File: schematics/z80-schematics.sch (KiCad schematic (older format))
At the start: 46 parts, among them P1 FTDI SERIAL, SW1 SW_PUSH, SW2 SW_PUSH, U1 Z80-CPU, U10 Z80-CTC, U11 Z80-SIO/0, U12 74HC574, U13 74HC541, U2 AS6C1008, U3 CAT28C256BL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

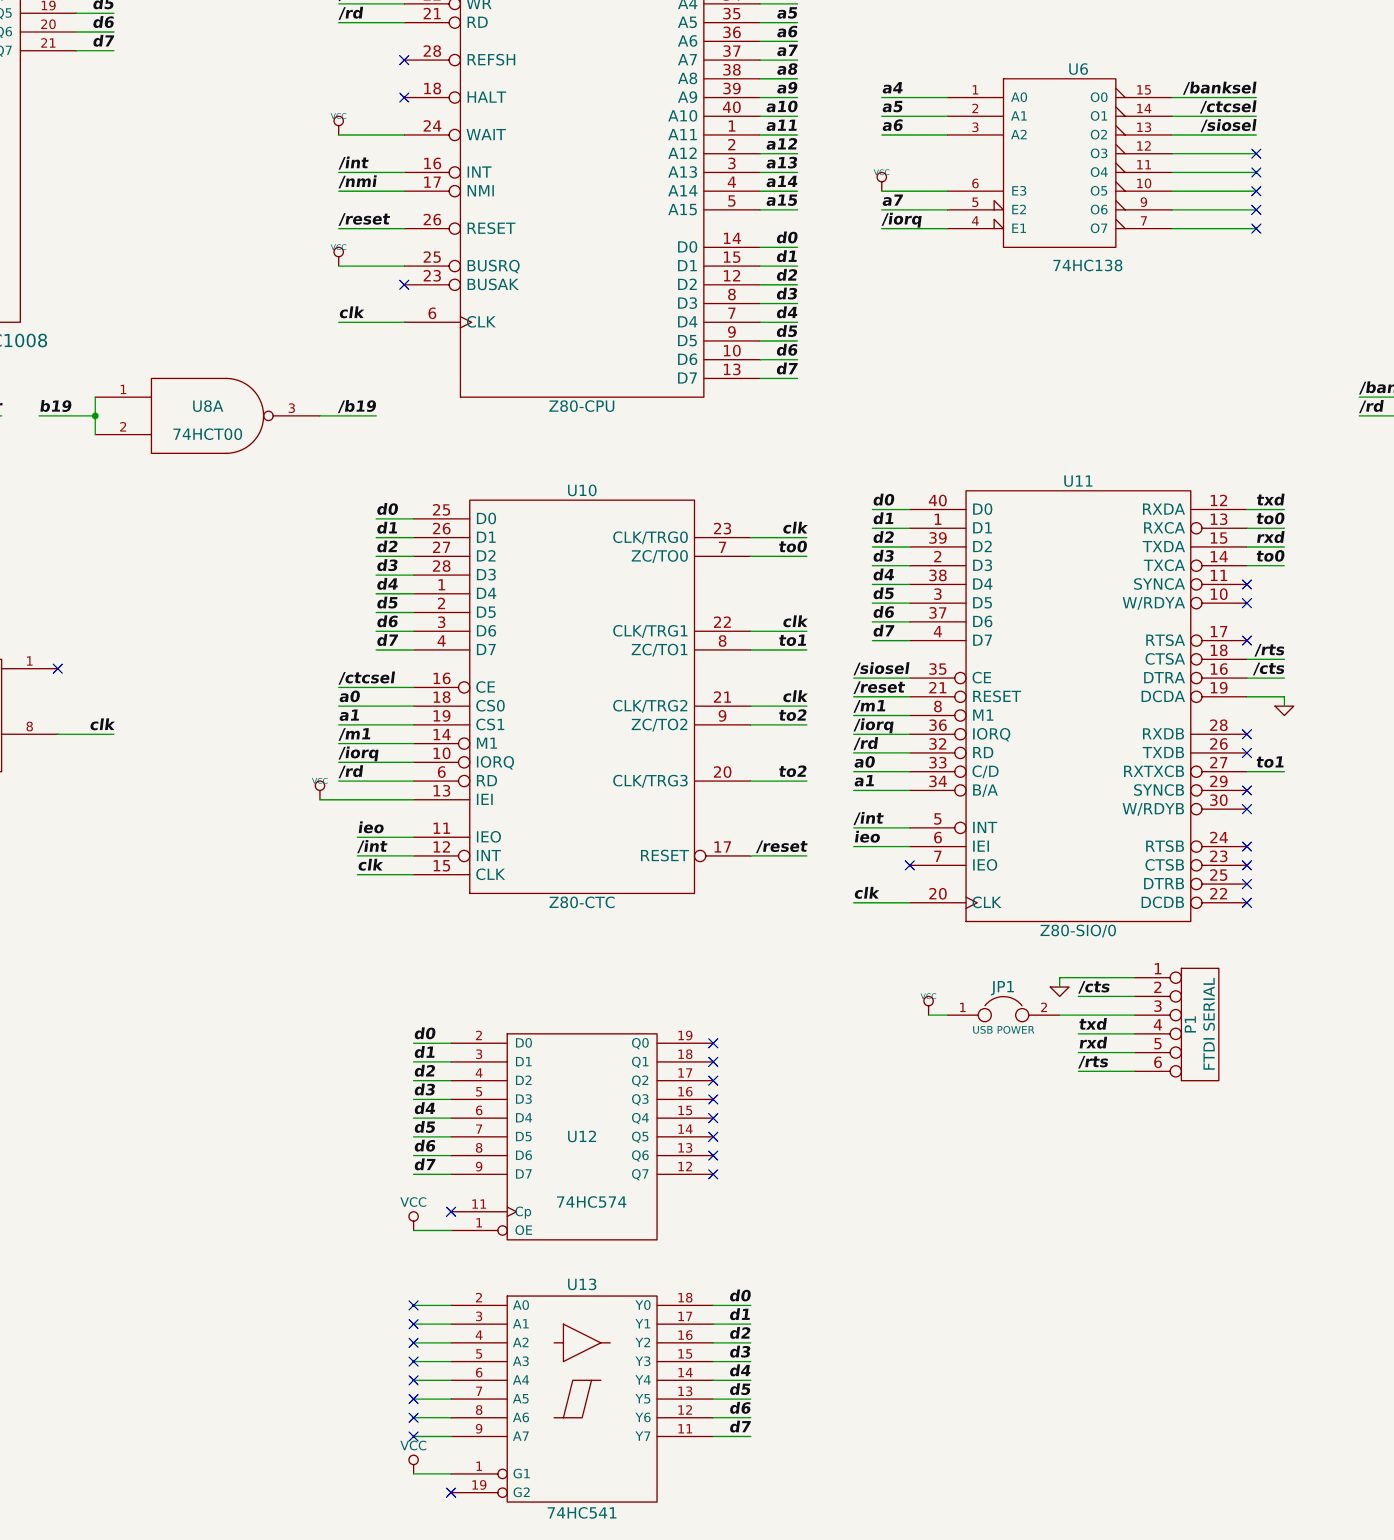
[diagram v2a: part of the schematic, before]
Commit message: Enabled parallel I/O ports
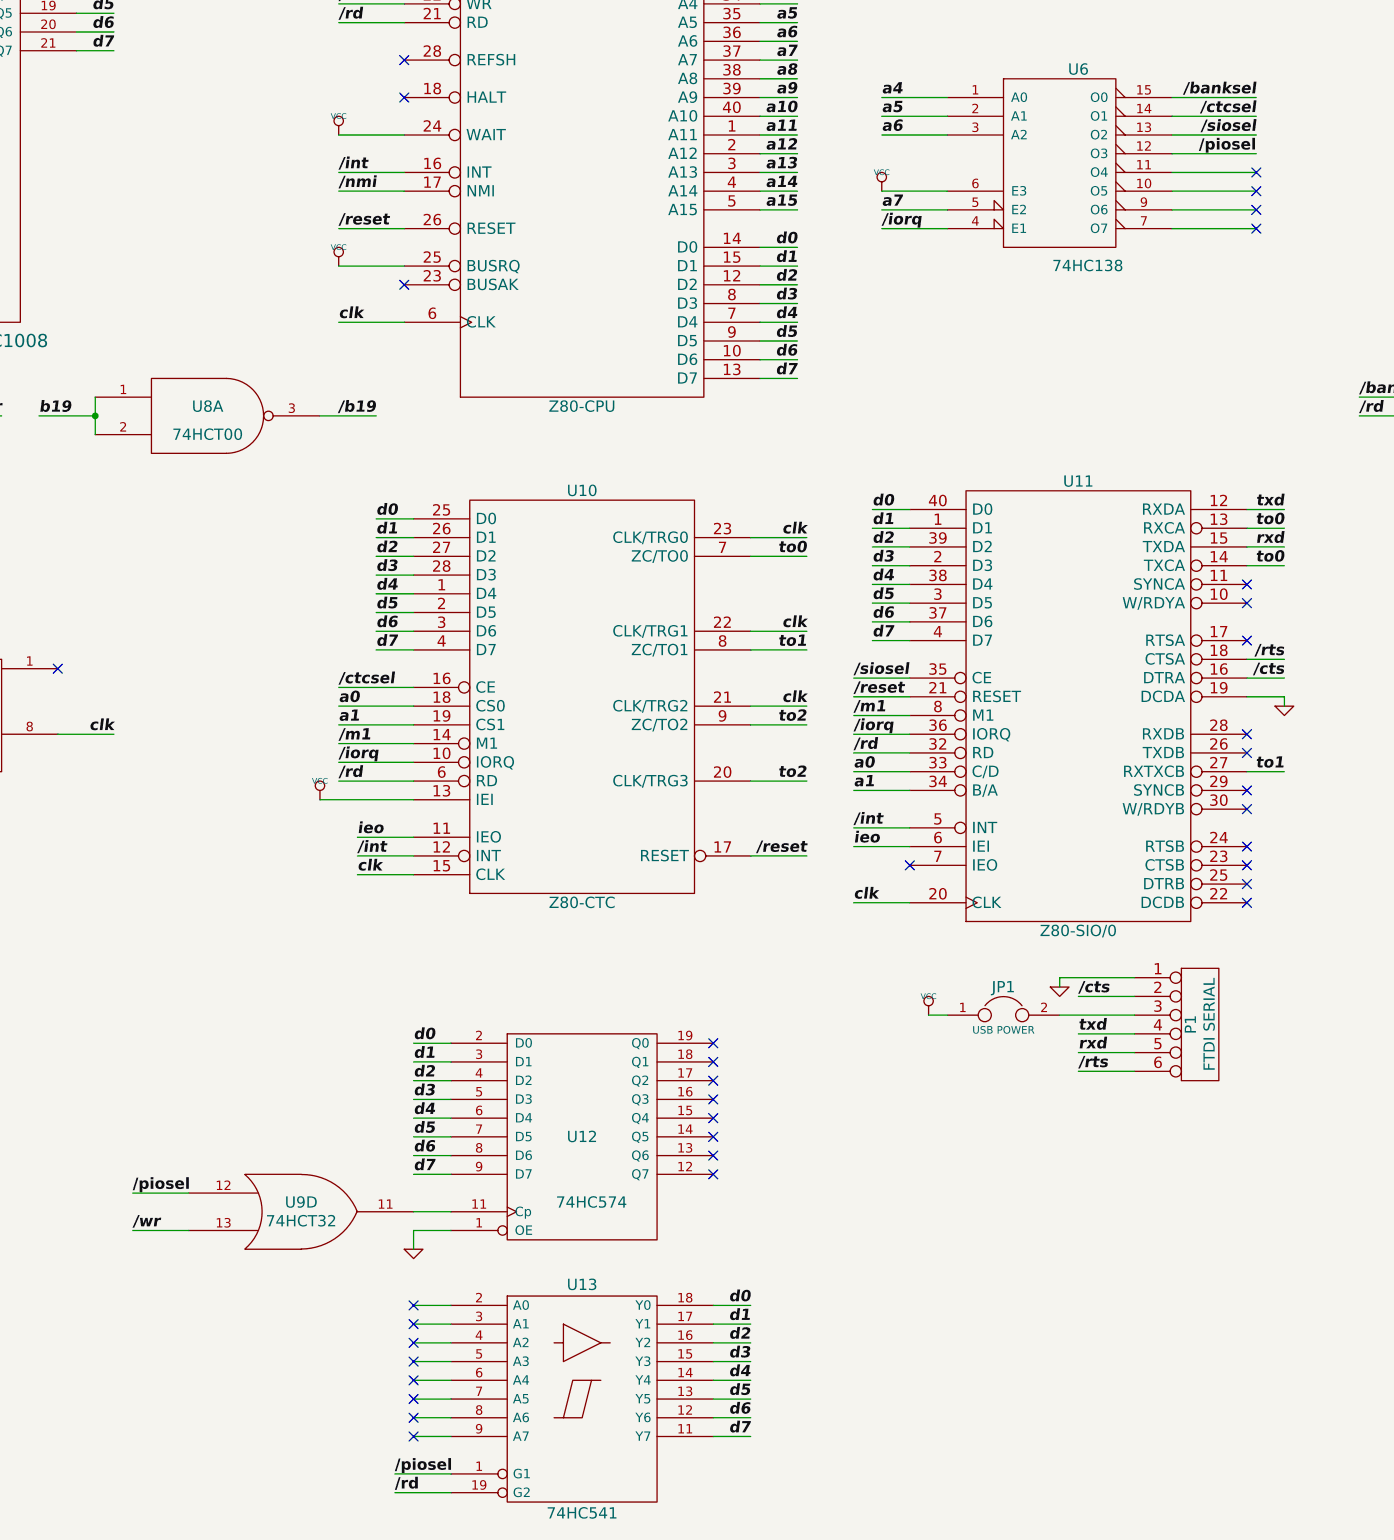
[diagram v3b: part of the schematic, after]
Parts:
- added unit 4 of U9
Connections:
- net +5V: now also U9.14 (VCC); no longer U12.1 (OE), U13.1 (G1)
- net /rd: now also U13.19 (G2)
- net /wr: now also U9.13
- net GND: now also U12.1 (OE), U9.7 (GND)
- net /piosel: now reaches U6.12 (O3)
- net /piosel: now also U13.1 (G1), U9.12
- net at U12.11 (Cp): now also U9.11
- no-connect marks 39 -> 36
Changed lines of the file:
@@
-	1    0    0    -1
-$EndComp
-$Comp
-L GND-RESCUE-z80-schematics #PWR07
-U 1 1 5439D0D3
-P 2250 6050
-F 0 "#PWR07" H 2250 6050 30  0001 C CNN
-F 1 "GND" H 2250 5980 30  0001 C CNN
-F 2 "" H 2250 6050 60  0000 C CNN
-F 3 "" H 2250 6050 60  0000 C CNN
-	1    2250 6050
 	1    0    0    -1
 $EndComp
@@
 /reset
 $Comp
-L VCC #PWR08
+L VCC #PWR07
 U 1 1 5439D481
 P 1550 4250
-F 0 "#PWR08" H 1550 4350 30  0001 C CNN
+F 0 "#PWR07" H 1550 4350 30  0001 C CNN
 F 1 "VCC" H 1550 4350 30  0000 C CNN
 F 2 "" H 1550 4250 60  0000 C CNN
@@
 $EndComp
 $Comp
-L GND-RESCUE-z80-schematics #PWR09
+L GND-RESCUE-z80-schematics #PWR08
 U 1 1 5439D495
 P 1550 6050
-F 0 "#PWR09" H 1550 6050 30  0001 C CNN
+F 0 "#PWR08" H 1550 6050 30  0001 C CNN
 F 1 "GND" H 1550 5980 30  0001 C CNN
 F 2 "" H 1550 6050 60  0000 C CNN
@@
 /nmi
 $Comp
-L VCC #PWR010
+L VCC #PWR09
 U 1 1 5439D74E
 P 1000 4250
-F 0 "#PWR010" H 1000 4350 30  0001 C CNN
+F 0 "#PWR09" H 1000 4350 30  0001 C CNN
 F 1 "VCC" H 1000 4350 30  0000 C CNN
 F 2 "" H 1000 4250 60  0000 C CNN
@@
 $EndComp
 $Comp
-L GND-RESCUE-z80-schematics #PWR011
+L GND-RESCUE-z80-schematics #PWR010
 U 1 1 5439D762
 P 1000 6050
-F 0 "#PWR011" H 1000 6050 30  0001 C CNN
+F 0 "#PWR010" H 1000 6050 30  0001 C CNN
 F 1 "GND" H 1000 5980 30  0001 C CNN
 F 2 "" H 1000 6050 60  0000 C CNN
@@
 $EndComp
 $Comp
-L GND-RESCUE-z80-schematics #PWR012
+L GND-RESCUE-z80-schematics #PWR011
 U 1 1 5439DA28
 P 3500 6050
-F 0 "#PWR012" H 3500 6050 30  0001 C CNN
+F 0 "#PWR011" H 3500 6050 30  0001 C CNN
 F 1 "GND" H 3500 5980 30  0001 C CNN
 F 2 "" H 3500 6050 60  0000 C CNN
@@
 $EndComp
 $Comp
-L VCC #PWR013
+L VCC #PWR012
 U 1 1 5439DA3C
 P 3500 4250
-F 0 "#PWR013" H 3500 4350 30  0001 C CNN
+F 0 "#PWR012" H 3500 4350 30  0001 C CNN
 F 1 "VCC" H 3500 4350 30  0000 C CNN
 F 2 "" H 3500 4250 60  0000 C CNN
@@
 /int
 $Comp
-L VCC #PWR014
+L VCC #PWR013
 U 1 1 54443902
 P 6200 5500
-F 0 "#PWR014" H 6200 5600 30  0001 C CNN
+F 0 "#PWR013" H 6200 5600 30  0001 C CNN
 F 1 "VCC" H 6200 5600 30  0000 C CNN
 F 2 "" H 6200 5500 60  0000 C CNN
@@
 /m1
 $Comp
-L VCC #PWR015
+L VCC #PWR014
 U 1 1 54443E22
 P 3000 4250
-F 0 "#PWR015" H 3000 4350 30  0001 C CNN
+F 0 "#PWR014" H 3000 4350 30  0001 C CNN
 F 1 "VCC" H 3000 4350 30  0000 C CNN
 F 2 "" H 3000 4250 60  0000 C CNN
@@
 $EndComp
 $Comp
-L GND-RESCUE-z80-schematics #PWR016
+L GND-RESCUE-z80-schematics #PWR015
 U 1 1 54444BB8
 P 10150 6500
-F 0 "#PWR016" H 10150 6500 30  0001 C CNN
+F 0 "#PWR015" H 10150 6500 30  0001 C CNN
 F 1 "GND" H 10150 6430 30  0001 C CNN
 F 2 "" H 10150 6500 60  0000 C CNN
@@
 /rts
 $Comp
-L VCC #PWR017
+L VCC #PWR016
 U 1 1 5444534D
 P 9450 6650
-F 0 "#PWR017" H 9450 6750 30  0001 C CNN
+F 0 "#PWR016" H 9450 6750 30  0001 C CNN
 F 1 "VCC" H 9450 6750 30  0000 C CNN
 F 2 "" H 9450 6650 60  0000 C CNN
@@
 /rts
 $Comp
-L GND-RESCUE-z80-schematics #PWR018
+L GND-RESCUE-z80-schematics #PWR017
 U 1 1 54445AE6
 P 11350 5000
-F 0 "#PWR018" H 11350 5000 30  0001 C CNN
+F 0 "#PWR017" H 11350 5000 30  0001 C CNN
 F 1 "GND" H 11350 4930 30  0001 C CNN
 F 2 "" H 11350 5000 60  0000 C CNN
@@
 $EndComp
 $Comp
-L VCC #PWR019
+L VCC #PWR018
 U 1 1 544499A7
 P 1900 6400
-F 0 "#PWR019" H 1900 6500 30  0001 C CNN
+F 0 "#PWR018" H 1900 6500 30  0001 C CNN
 F 1 "VCC" H 1900 6500 30  0000 C CNN
 F 2 "" H 1900 6400 60  0000 C CNN
@@
 $EndComp
 $Comp
-L GND-RESCUE-z80-schematics #PWR020
+L GND-RESCUE-z80-schematics #PWR019
 U 1 1 54449B07
 P 1900 7200
-F 0 "#PWR020" H 1900 7200 30  0001 C CNN
+F 0 "#PWR019" H 1900 7200 30  0001 C CNN
 F 1 "GND" H 1900 7130 30  0001 C CNN
 F 2 "" H 1900 7200 60  0000 C CNN
@@
 $EndComp
 $Comp
-L VCC #PWR021
+L VCC #PWR020
 U 1 1 5444AC97
 P 1900 7400
-F 0 "#PWR021" H 1900 7500 30  0001 C CNN
+F 0 "#PWR020" H 1900 7500 30  0001 C CNN
 F 1 "VCC" H 1900 7500 30  0000 C CNN
 F 2 "" H 1900 7400 60  0000 C CNN
@@
 $EndComp
 $Comp
-L GND-RESCUE-z80-schematics #PWR022
+L GND-RESCUE-z80-schematics #PWR021
 U 1 1 5444ACAB
 P 1900 8200
-F 0 "#PWR022" H 1900 8200 30  0001 C CNN
+F 0 "#PWR021" H 1900 8200 30  0001 C CNN
 F 1 "GND" H 1900 8130 30  0001 C CNN
 F 2 "" H 1900 8200 60  0000 C CNN
@@
 Text Label 6300 2950 0    60   Italic 12
 clk
-NoConn ~ 11200 2050
-NoConn ~ 11200 2150
 NoConn ~ 11200 2250
 NoConn ~ 11200 2350
@@
 	1550 5800 1550 6050
 $Comp
-L VCC #PWR023
+L VCC #PWR022
 U 1 1 5727041A
 P 3300 6500
-F 0 "#PWR023" H 3300 6350 50  0001 C CNN
+F 0 "#PWR022" H 3300 6350 50  0001 C CNN
 F 1 "VCC" H 3300 6650 50  0000 C CNN
 F 2 "" H 3300 6500 50  0000 C CNN
@@
 $EndComp
 $Comp
-L +5V #PWR024
+L +5V #PWR023
 U 1 1 572704C1
 P 3500 6500
-F 0 "#PWR024" H 3500 6350 50  0001 C CNN
+F 0 "#PWR023" H 3500 6350 50  0001 C CNN
 F 1 "+5V" H 3500 6640 50  0000 C CNN
 F 2 "" H 3500 6500 50  0000 C CNN
@@
 	3500 6600 3500 6500
 $Comp
-L GND #PWR025
+L GND #PWR024
 U 1 1 57270C2C
 P 3300 7100
-F 0 "#PWR025" H 3300 6850 50  0001 C CNN
+F 0 "#PWR024" H 3300 6850 50  0001 C CNN
 F 1 "GND" H 3300 6950 50  0000 C CNN
 F 2 "" H 3300 7100 50  0000 C CNN
@@
 $EndComp
 $Comp
-L VSS #PWR026
+L VSS #PWR025
 U 1 1 57271C85
 P 3500 7100
-F 0 "#PWR026" H 3500 6950 50  0001 C CNN
+F 0 "#PWR025" H 3500 6950 50  0001 C CNN
 F 1 "VSS" H 3500 7250 50  0000 C CNN
 F 2 "" H 3500 7100 50  0000 C CNN
@@
 	3500 4850 3500 4250
 $Comp
-L PWR_FLAG #FLG027
+L PWR_FLAG #FLG026
 U 1 1 57273DF5
 P 3750 6500
-F 0 "#FLG027" H 3750 6595 50  0001 C CNN
+F 0 "#FLG026" H 3750 6595 50  0001 C CNN
 F 1 "PWR_FLAG" H 3750 6680 50  0000 C CNN
 F 2 "" H 3750 6500 50  0000 C CNN
@@
 Connection ~ 3500 6600
 $Comp
-L PWR_FLAG #FLG028
+L PWR_FLAG #FLG027
 U 1 1 57274482
 P 3750 7100
-F 0 "#FLG028" H 3750 7195 50  0001 C CNN
+F 0 "#FLG027" H 3750 7195 50  0001 C CNN
 F 1 "PWR_FLAG" H 3750 7280 50  0000 C CNN
 F 2 "" H 3750 7100 50  0000 C CNN
@@
 	3750 7000 3750 7100
 Connection ~ 3500 7000
-$Comp
-L VCC #PWR029
-U 1 1 5725E77F
-P 6700 7800
-F 0 "#PWR029" H 6700 7650 50  0001 C CNN
-F 1 "VCC" H 6700 7950 50  0000 C CNN
-F 2 "" H 6700 7800 50  0000 C CNN
-F 3 "" H 6700 7800 50  0000 C CNN
-	1    6700 7800
-	1    0    0    -1
-$EndComp
-Wire Wire Line
-	6900 7800 6700 7800
-NoConn ~ 6900 7700
-$Comp
-L VCC #PWR030
-U 1 1 5725EC6B
-P 6700 9100
-F 0 "#PWR030" H 6700 8950 50  0001 C CNN
-F 1 "VCC" H 6700 9250 50  0000 C CNN
-F 2 "" H 6700 9100 50  0000 C CNN
-F 3 "" H 6700 9100 50  0000 C CNN
-	1    6700 9100
-	1    0    0    -1
-$EndComp
-Wire Wire Line
-	6700 9100 6900 9100
-NoConn ~ 6900 9200
 $Comp
 L 74LS32 U9
@@
 Text Label 8800 5000 2    60   Italic 12
 clk
+Text Label 11200 2050 2    60   ~ 12
+/piosel
+Wire Wire Line
+	6900 7700 6700 7700
+$Comp
+L GND-RESCUE-z80-schematics #PWR028
+U 1 1 5439D0D3
+P 2250 6050
+F 0 "#PWR028" H 2250 6050 30  0001 C CNN
+F 1 "GND" H 2250 5980 30  0001 C CNN
+F 2 "" H 2250 6050 60  0000 C CNN
+F 3 "" H 2250 6050 60  0000 C CNN
+	1    2250 6050
+	1    0    0    -1
+$EndComp
+$Comp
+L GND-RESCUE-z80-schematics #PWR029
+U 1 1 574F0B67
+P 6700 7900
+F 0 "#PWR029" H 6700 7900 30  0001 C CNN
+F 1 "GND" H 6700 7830 30  0001 C CNN
+F 2 "" H 6700 7900 60  0000 C CNN
+F 3 "" H 6700 7900 60  0000 C CNN
+	1    6700 7900
+	1    0    0    -1
+$EndComp
+Wire Wire Line
+	6900 7800 6700 7800
+Wire Wire Line
+	6700 7800 6700 7900
+Text Label 6600 9100 0    60   ~ 12
+/piosel
+Text Label 6600 9200 0    60   ~ 12
+/rd
+$Comp
+L 74LS32 U9
+U 4 1 574F5D51
+P 6100 7700
+F 0 "U9" H 6100 7750 60  0000 C CNN
+F 1 "74HCT32" H 6100 7650 60  0000 C CNN
+F 2 "~" H 6100 7700 60  0000 C CNN
+F 3 "~" H 6100 7700 60  0000 C CNN
+	4    6100 7700
+	1    0    0    -1
+$EndComp
+Text Label 5200 7800 0    60   Italic 12
+/wr
+Text Label 5200 7600 0    60   ~ 12
+/piosel
+NoConn ~ 11200 2150
+Wire Wire Line
+	6600 9100 6900 9100
+Wire Wire Line
+	6600 9200 6900 9200
+Wire Wire Line
+	5500 7600 5200 7600
+Wire Wire Line
+	5200 7800 5500 7800
 $EndSCHEMATC

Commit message: Added schematics for SD card interfacing
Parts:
- added P2: CONN_02X08, symbol CONN_02X08
- added R13, R14, R15, R16, R17, R18, R19, R20: 10k, ~, symbol R-RESCUE-z80-schematics
- added unit 4 of U8
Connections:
- net +5V: now also P2.13 (P13), P2.14 (P14), R13.1, R14.1, U8.14 (VCC)
- net GND: now also P2.1 (P1), P2.15 (P15), P2.16 (P16), P2.2 (P2), R16.2, R18.2, R20.2, U8.7 (GND)
- net nss5: now reaches U12.17 (Q2)
- net nss5: now also R19.2
- net sck5: now reaches U12.18 (Q1)
- net sck5: now also R17.2
- net miso5: now reaches U12.19 (Q0)
- net miso5: now also R15.2
- net at U13.2 (A0): now also U8.11
- net c_cd: now reaches U13.3 (A1)
- net c_cd: now also P2.7 (P7), R13.2
- net c_wp: now reaches U13.4 (A2)
- net c_wp: now also P2.5 (P5), R14.2
- new net 3.3v: P2.3 (P3), P2.4 (P4)
- new net data1: P2.11 (P11)
- new net data2: P2.9 (P9)
- new net miso: P2.8 (P8), R15.1, R16.1
- new net mosi: P2.10 (P10), U8.12, U8.13
- new net nss: P2.12 (P12), R19.1, R20.1
- new net sck: P2.6 (P6), R17.1, R18.1
- no-connect marks 36 -> 32
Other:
- moved on the sheet: U13

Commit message: Add support for second serial port in the schematics
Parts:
- added P?: CONN_01X06, symbol CONN_01X06
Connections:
- net labels added: /cts2, /rts2, rxd2, txd2
- wire segments 386 -> 397
- no-connect marks 32 -> 28
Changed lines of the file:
@@
 $EndComp
 NoConn ~ 11150 6050
-NoConn ~ 11150 5850
-NoConn ~ 11150 5750
 NoConn ~ 11150 5950
-NoConn ~ 11150 5250
-NoConn ~ 11150 5150
 NoConn ~ 11150 5450
 NoConn ~ 11150 5550
@@
 Text Label 14300 8400 0    60   Italic 12
 nss5
+$Comp
+L CONN_01X06 P?
+U 1 1 57BA2236
+P 10900 7550
+F 0 "P?" H 10900 7900 50  0000 C CNN
+F 1 "CONN_01X06" V 11000 7550 50  0000 C CNN
+F 2 "" H 10900 7550 50  0000 C CNN
+F 3 "" H 10900 7550 50  0000 C CNN
+	1    10900 7550
+	1    0    0    -1
+$EndComp
+Wire Wire Line
+	10700 7300 10200 7300
+$Comp
+L VCC #PWR?
+U 1 1 57BA27E4
+P 10200 7300
+F 0 "#PWR?" H 10200 7400 30  0001 C CNN
+F 1 "VCC" H 10200 7400 30  0000 C CNN
+F 2 "" H 10200 7300 60  0000 C CNN
+F 3 "" H 10200 7300 60  0000 C CNN
+	1    10200 7300
+	1    0    0    -1
+$EndComp
+Wire Wire Line
+	10700 7600 10200 7600
+$Comp
+L GND-RESCUE-z80-schematics #PWR?
+U 1 1 57BA2A97
+P 10200 7650
+F 0 "#PWR?" H 10200 7650 30  0001 C CNN
+F 1 "GND" H 10200 7580 30  0001 C CNN
+F 2 "" H 10200 7650 60  0000 C CNN
+F 3 "" H 10200 7650 60  0000 C CNN
+	1    10200 7650
+	1    0    0    -1
+$EndComp
+Wire Wire Line
+	10200 7600 10200 7650
+Wire Wire Line
+	11150 5150 11350 5150
+Text Label 11350 5150 2    60   Italic 12
+txd2
+Wire Wire Line
+	11150 5250 11350 5250
+Text Label 11350 5250 2    60   Italic 12
+rxd2
+Wire Wire Line
+	10700 7400 10300 7400
+Text Label 10300 7400 0    60   Italic 12
+rxd2
+Wire Wire Line
+	10700 7500 10300 7500
+Text Label 10300 7500 0    60   Italic 12
+txd2
+Wire Wire Line
+	11150 5750 11350 5750
+Wire Wire Line
+	11150 5850 11350 5850
+Text Label 11350 5750 2    60   Italic 12
+/cts2
+Text Label 11350 5850 2    60   Italic 12
+/rts2
+Wire Wire Line
+	10700 7700 10300 7700
+Text Label 10300 7700 0    60   Italic 12
+/cts2
+Wire Wire Line
+	10700 7800 10300 7800
+Text Label 10300 7800 0    60   Italic 12
+/rts2
 $EndSCHEMATC
